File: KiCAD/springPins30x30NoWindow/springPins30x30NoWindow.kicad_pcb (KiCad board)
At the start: 2 copper layers, 30 x 30 mm, 22 parts, among them J1 CONN_02X06, J2 CONN_02X06

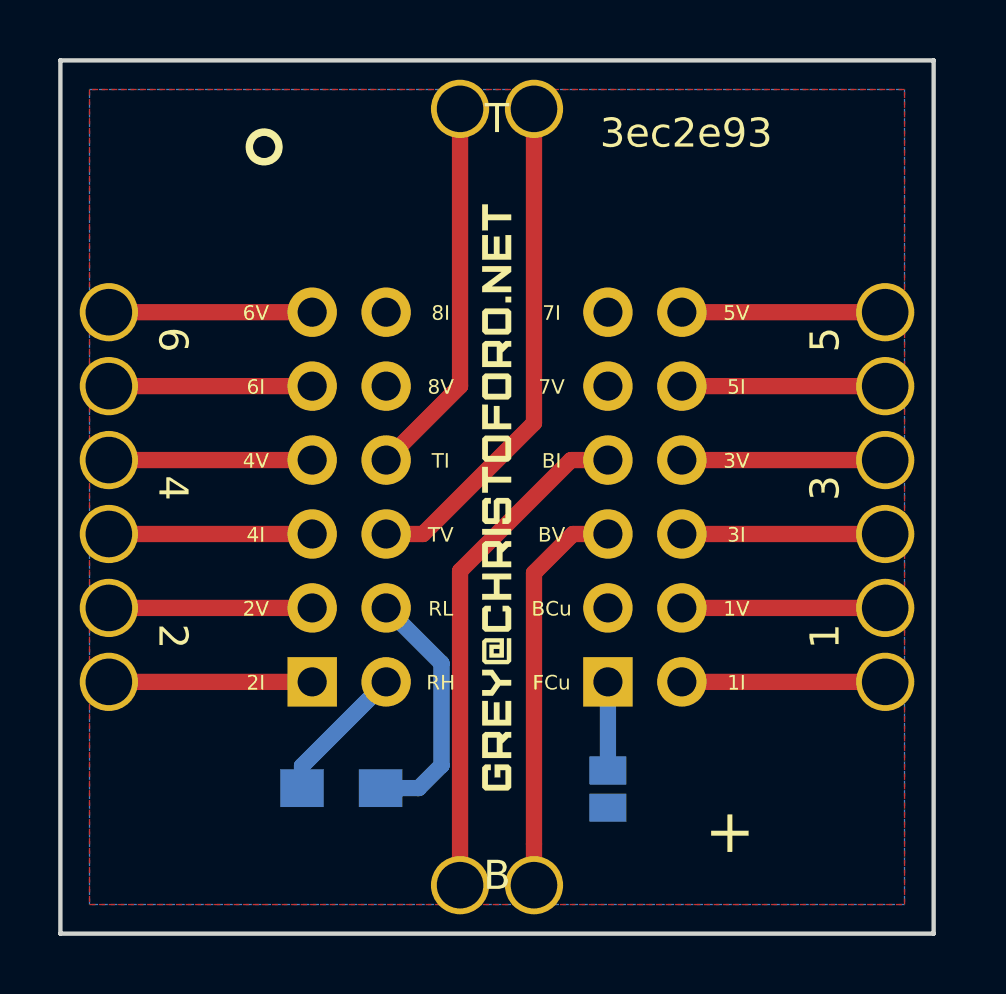
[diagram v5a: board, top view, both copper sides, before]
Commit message: starting on ethercat board pin boards rotated base1x zones fixed
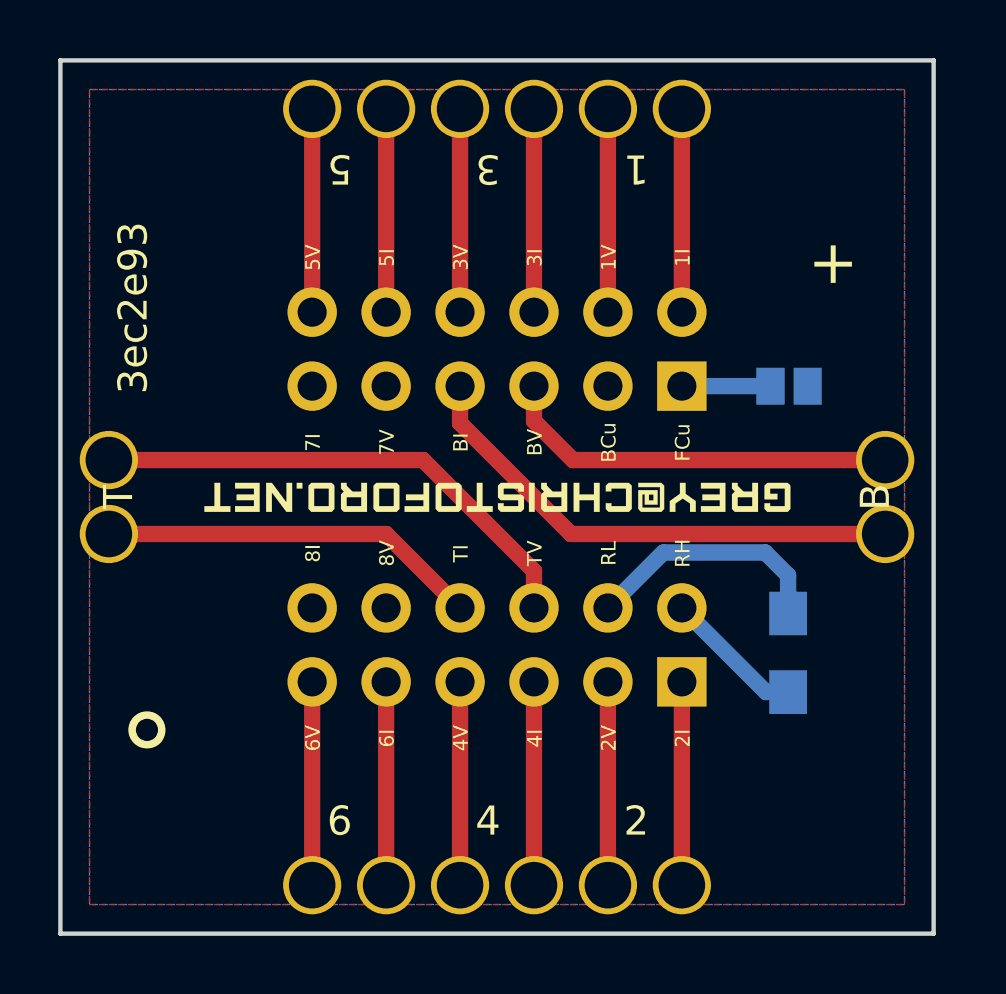
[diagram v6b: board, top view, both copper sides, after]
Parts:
- moved TP15 20.9 mm to (-6.35, -13.3), turned to 90 degrees
- moved TP20 20.9 mm to (6.35, -13.3), turned to 90 degrees
- moved TP3 20.9 mm to (-6.35, 13.3), turned to 90 degrees
- moved TP8 20.9 mm to (6.35, 13.3), turned to 90 degrees
- moved TP16 19.6 mm to (-3.81, -13.3), turned to 90 degrees
- moved TP19 19.6 mm to (3.81, -13.3), turned to 90 degrees
- moved TP4 19.6 mm to (-3.81, 13.3), turned to 90 degrees
- moved TP7 19.6 mm to (3.81, 13.3), turned to 90 degrees
- moved TP10 18.9 mm to (13.3, 1.27), turned to 90 degrees
- moved TP11 18.9 mm to (-13.3, -1.27), turned to 90 degrees
- moved TP12 18.9 mm to (13.3, -1.27), turned to 90 degrees
- moved TP17 18.9 mm to (-1.27, -13.3), turned to 90 degrees
- moved TP18 18.9 mm to (1.27, -13.3), turned to 90 degrees
- moved TP5 18.9 mm to (-1.27, 13.3), turned to 90 degrees
- moved TP6 18.9 mm to (1.27, 13.3), turned to 90 degrees
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
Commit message: update silk
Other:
- board text added: "20b2bb8"
- board text removed: "3ec2e93"
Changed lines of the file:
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@@
-(kicad_pcb (version 20171130) (host pcbnew "(5.0-dev-4085-g9241a399a)")
+(kicad_pcb (version 20171130) (host pcbnew "(5.0.0-rc2-dev-44-gde6b32d23)")
   (general
     (thickness 1.6)
@@
       (usegerberattributes true)
       (usegerberadvancedattributes true)
-      (creategerberjobfile true)
+      (creategerberjobfile false)
       (excludeedgelayer true)
       (linewidth 0.150000)
@@
     (effects (font (size 1 1) (thickness 0.25)))
   )
-  (gr_text 3ec2e93 (at -12.5 -6.5 90) (layer F.SilkS)
+  (gr_text 20b2bb8 (at -12.5 -6.5 90) (layer F.SilkS)
     (effects (font (size 1 1) (thickness 0.175)))
   )

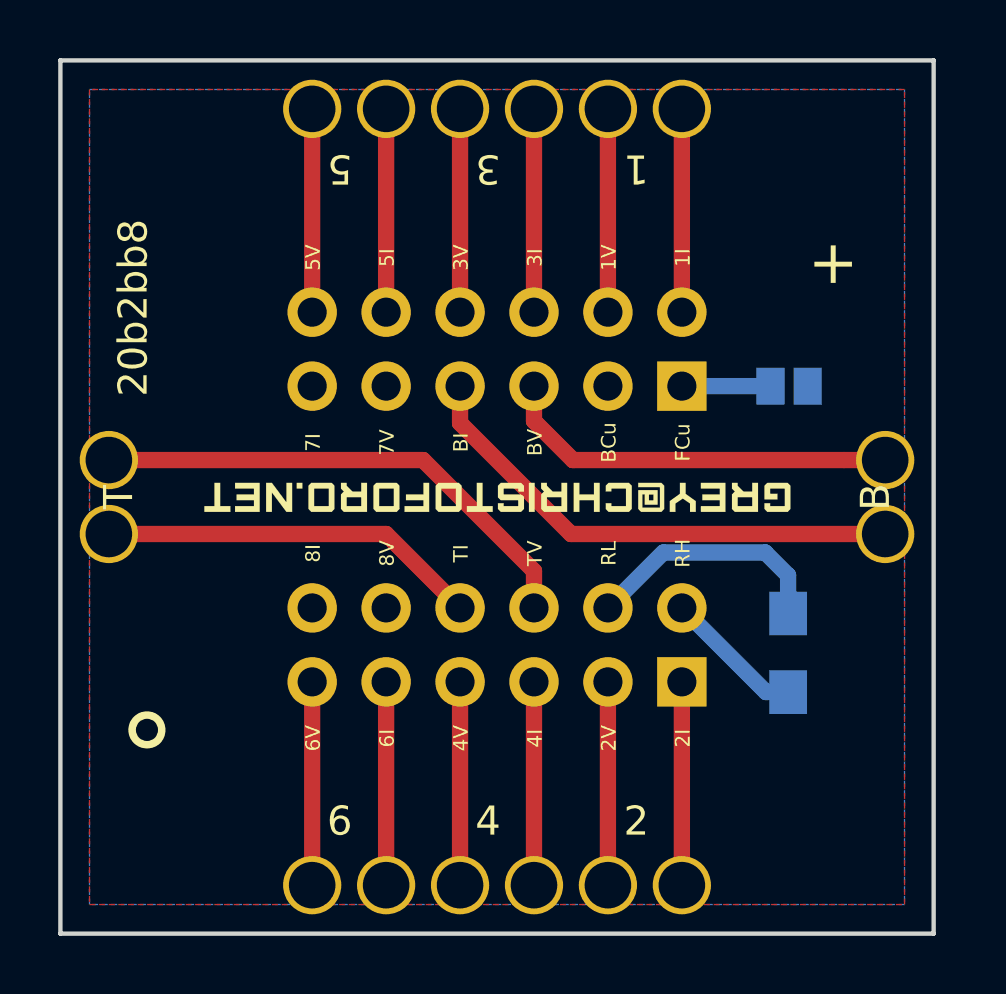
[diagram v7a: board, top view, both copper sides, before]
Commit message: add dbg substrate layout and 8x1 backplane
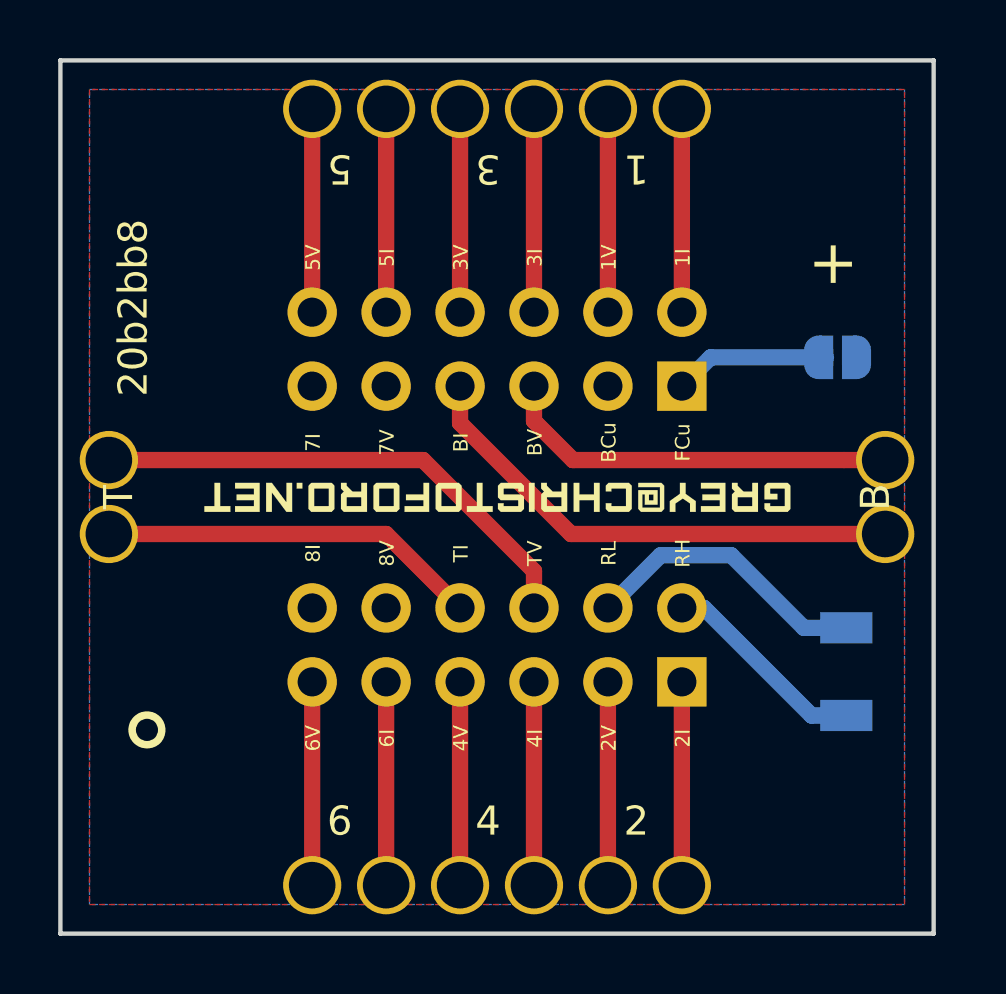
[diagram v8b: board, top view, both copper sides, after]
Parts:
- J1, J2: footprint Pin_Headers:Pin_Header_Straight_2x06_Pitch2.54mm -> Connector_PinHeader_2.54mm:PinHeader_2x06_P2.54mm_Vertical
- JP1: footprint Connectors:GS2 -> Jumper:SolderJumper-2_P1.3mm_Open_RoundedPad1.0x1.5mm
- R1: footprint Resistors_SMD:R_0805_HandSoldering -> Resistor_SMD:R_1206_3216Metric
- moved R1 2.10 mm to (12.0, 6.00)
- moved JP1 1.94 mm to (11.7, -4.80), turned to 180 degrees
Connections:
- J1 pad 10: (no net) -> Net-(J1-Pad10)
- J1 pad 12: (no net) -> Net-(J1-Pad12)
- J2 pad 11: (no net) -> Net-(J2-Pad11)
- J2 pad 9: (no net) -> Net-(J2-Pad9)
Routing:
- net /RH: track 4.85 -> 7.18 mm
- net /FCu: track 3.04 -> 5.36 mm
- net /RL: track 8.61 -> 9.97 mm
